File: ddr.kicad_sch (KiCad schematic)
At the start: 79 parts, among them U801 MT41K256M16TW

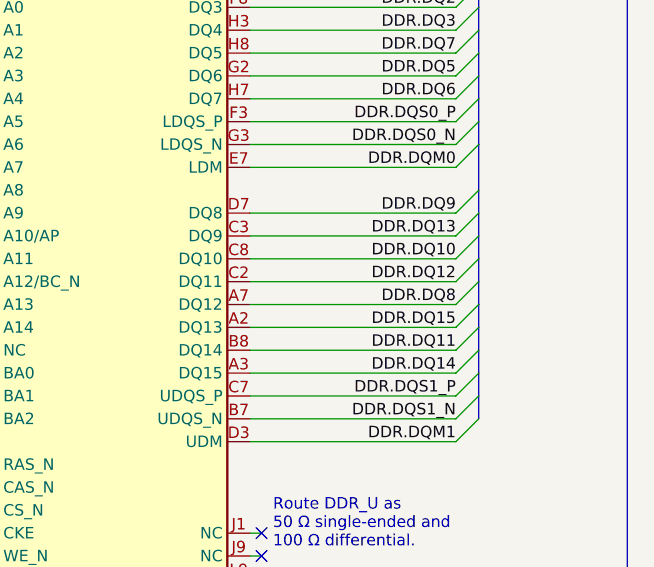
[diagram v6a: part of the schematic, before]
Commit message: Finish cleaner DDR routing
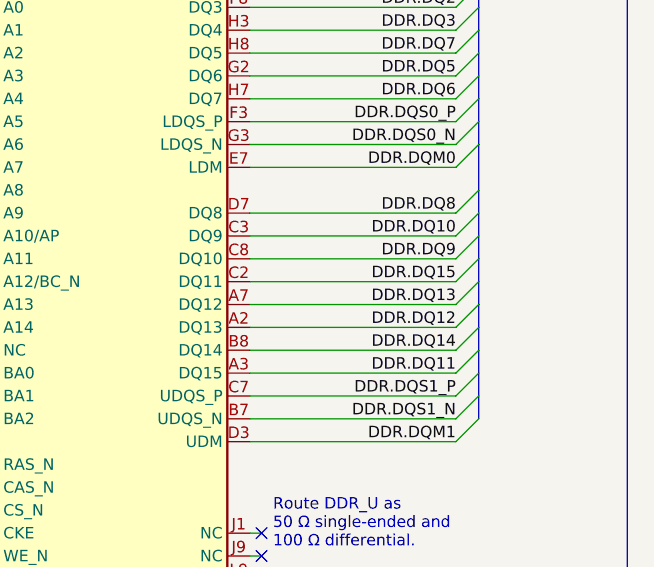
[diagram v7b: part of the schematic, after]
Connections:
- net DDR.DQ10: now also U801.C3 (DQ9); no longer U801.C8 (DQ10)
- net DDR.DQ11: now also U801.A3 (DQ15); no longer U801.B8 (DQ14)
- net DDR.DQ12: now also U801.A2 (DQ13); no longer U801.C2 (DQ11)
- net DDR.DQ13: now also U801.A7 (DQ12); no longer U801.C3 (DQ9)
- net DDR.DQ14: now also U801.B8 (DQ14); no longer U801.A3 (DQ15)
- net DDR.DQ15: now also U801.C2 (DQ11); no longer U801.A2 (DQ13)
- net DDR.DQ8: now also U801.D7 (DQ8); no longer U801.A7 (DQ12)
- net DDR.DQ9: now also U801.C8 (DQ10); no longer U801.D7 (DQ8)
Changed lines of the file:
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@@
 	)
 	(label "DDR.DQ13"
-		(at 387.35 132.08 180)
+		(at 387.35 139.7 180)
 		(effects
 			(font
@@
 	)
 	(label "DDR.DQ12"
-		(at 387.35 137.16 180)
+		(at 387.35 142.24 180)
 		(effects
 			(font
@@
 	)
 	(label "DDR.DQ14"
-		(at 387.35 147.32 180)
+		(at 387.35 144.78 180)
 		(effects
 			(font
@@
 	)
 	(label "DDR.DQ9"
-		(at 387.35 129.54 180)
+		(at 387.35 134.62 180)
 		(effects
 			(font
@@
 	)
 	(label "DDR.DQ11"
-		(at 387.35 144.78 180)
+		(at 387.35 147.32 180)
 		(effects
 			(font
@@
 	)
 	(label "DDR.DQ10"
-		(at 387.35 134.62 180)
+		(at 387.35 132.08 180)
 		(effects
 			(font
@@
 	)
 	(label "DDR.DQ15"
-		(at 387.35 142.24 180)
+		(at 387.35 137.16 180)
 		(effects
 			(font
@@
 	)
 	(label "DDR.DQ8"
-		(at 387.35 139.7 180)
-		(effects
-			(font
+		(at 387.35 129.54 180)
+		(effects
+			(font

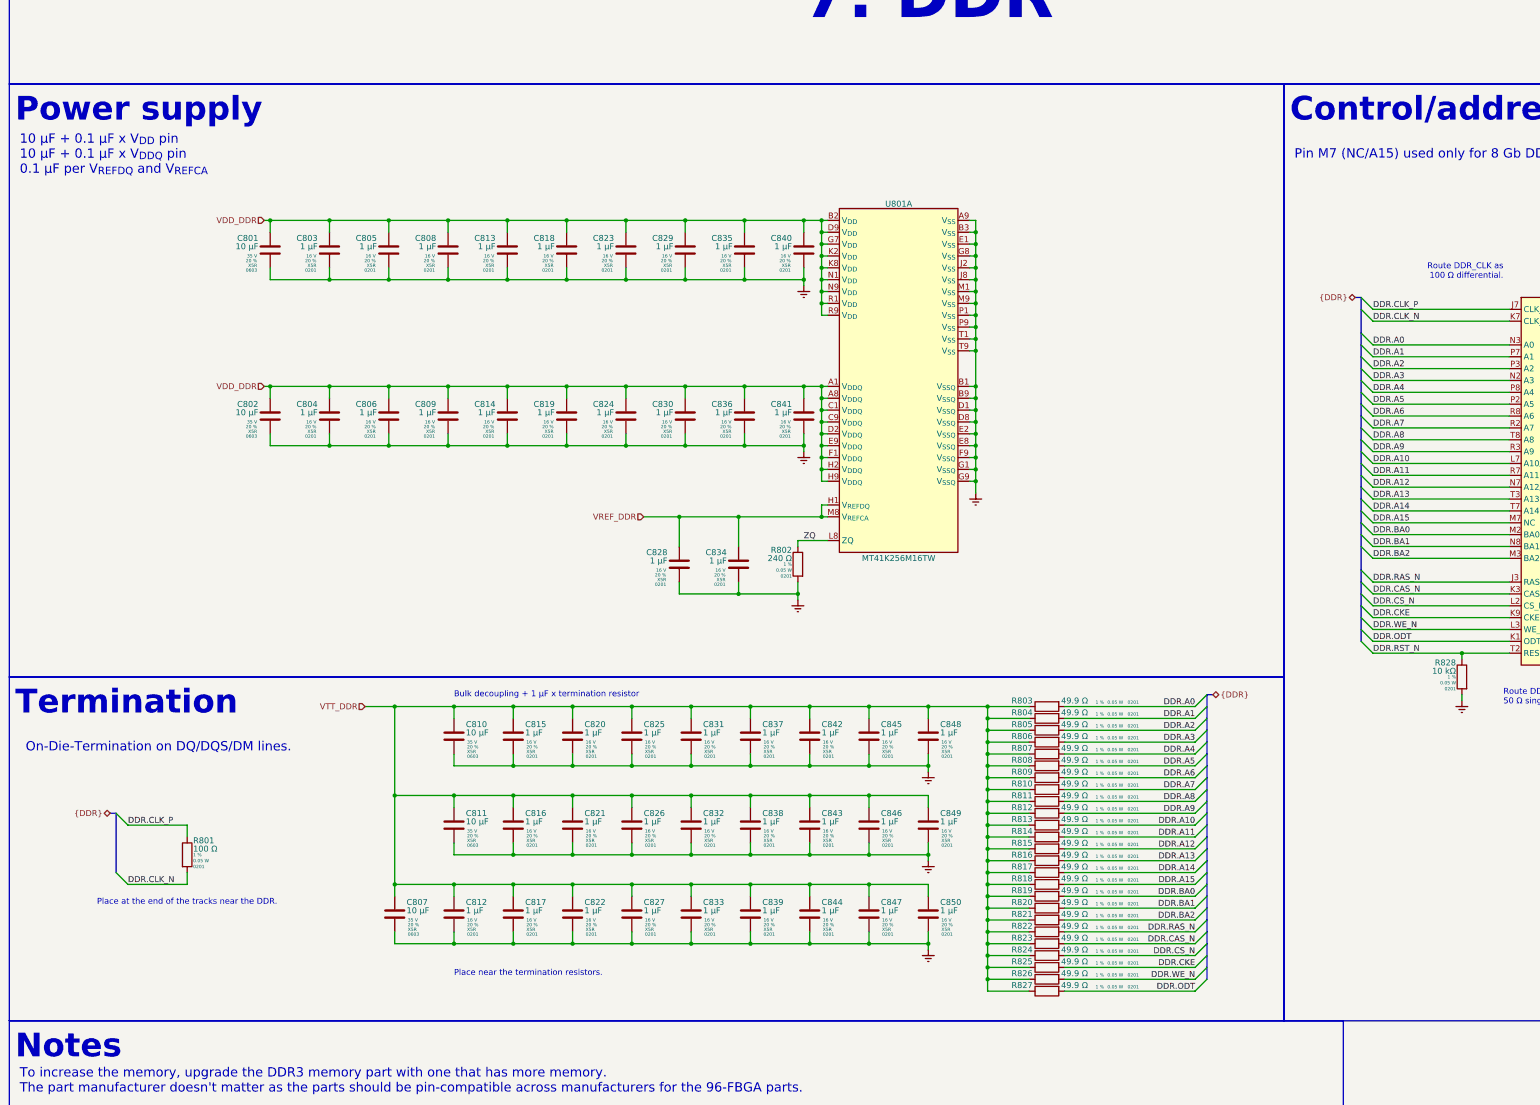
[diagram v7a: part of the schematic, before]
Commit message: Fallback to DDR series termination
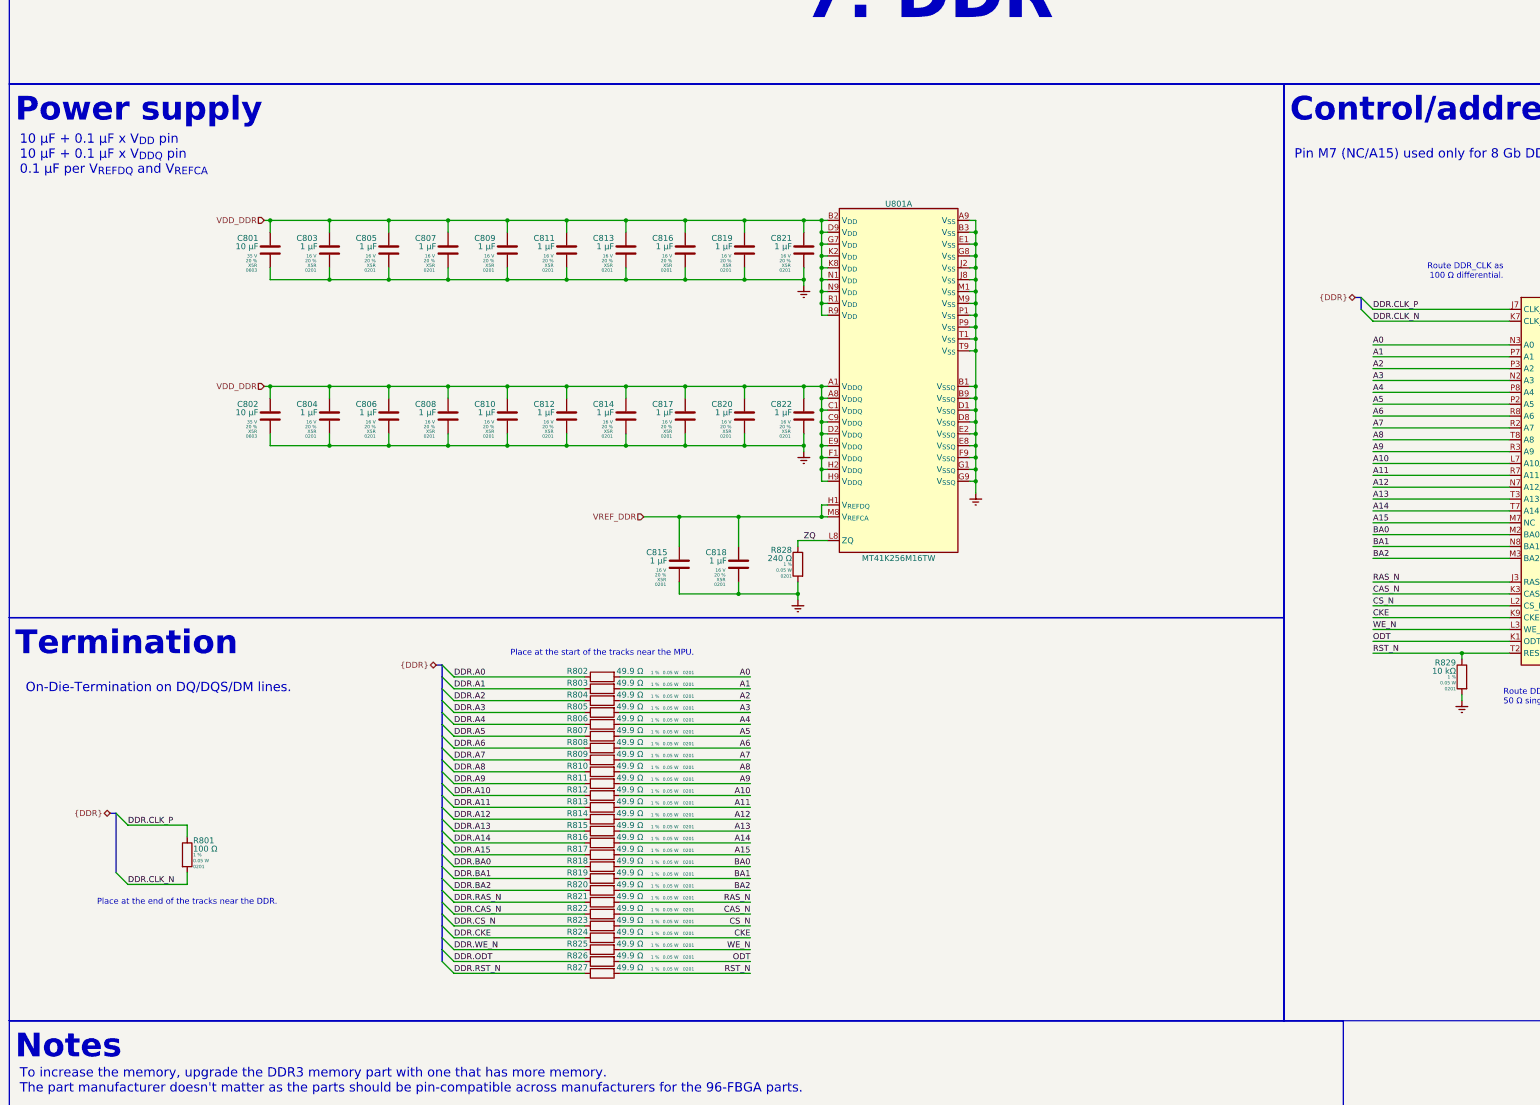
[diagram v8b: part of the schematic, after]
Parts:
- removed C807, C810, C811: 10 µF, Capacitor_SMD:C_0603_1608Metric, symbol Device:C
- removed C812, C815, C816, C817, C820, C821, C822, C825, C826, C827, C831, C832, C833, C837, C838, C839, C842, C843, C844, C845, C846, C847, C848, C849, C850: 1 µF, perfect_footprints:C_0201_0603Metric, symbol Device:C
- added R827: 49.9 Ω, perfect_footprints:R_0201_0603Metric, symbol Device:R
- renumbered C808 to C807, C809 to C808, C813 to C809, C814 to C810, C818 to C811, C819 to C812, C823 to C813, C824 to C814, C828 to C815, C829 to C816, C830 to C817, C834 to C818, C835 to C819, C836 to C820, C840 to C821, C841 to C822, R803 to R802, R804 to R803, R805 to R804, R806 to R805, R807 to R806, R808 to R807, R809 to R808, R810 to R809, R811 to R810, R812 to R811, R813 to R812, R814 to R813, R815 to R814, R816 to R815, R817 to R816, R818 to R817, R819 to R818, R820 to R819, R821 to R820, R822 to R821, R823 to R822, R824 to R823, R825 to R824, R826 to R825, R827 to R826, R802 to R828, R828 to R829
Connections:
- net DDR.A0: now also R802.1; no longer R802.2, U801.N3 (A0)
- net DDR.A1: now also R803.1; no longer R803.2, U801.P7 (A1)
- net DDR.A10: now also R812.1; no longer R812.2, U801.L7 (A10/AP)
- net DDR.A11: now also R813.1; no longer R813.2, U801.R7 (A11)
- net DDR.A12: now also R814.1; no longer R814.2, U801.N7 (A12/BC_N)
- net DDR.A13: now also R815.1; no longer R815.2, U801.T3 (A13)
- net DDR.A14: now also R816.1; no longer R816.2, U801.T7 (A14)
- net DDR.A15: now also R817.1; no longer R817.2, U801.M7 (NC)
- net DDR.A2: now also R804.1; no longer R804.2, U801.P3 (A2)
- net DDR.A3: now also R805.1; no longer R805.2, U801.N2 (A3)
- net DDR.A4: now also R806.1; no longer R806.2, U801.P8 (A4)
- net DDR.A5: now also R807.1; no longer R807.2, U801.P2 (A5)
- net DDR.A6: now also R808.1; no longer R808.2, U801.R8 (A6)
- net DDR.A7: now also R809.1; no longer R809.2, U801.R2 (A7)
- net DDR.A8: now also R810.1; no longer R810.2, U801.T8 (A8)
- net DDR.A9: now also R811.1; no longer R811.2, U801.R3 (A9)
- net DDR.BA0: now also R818.1; no longer R818.2, U801.M2 (BA0)
- net DDR.BA1: now also R819.1; no longer R819.2, U801.N8 (BA1)
- net DDR.BA2: now also R820.1; no longer R820.2, U801.M3 (BA2)
- net DDR.CAS_N: now also R822.1; no longer R822.2, U801.K3 (CAS_N)
- net DDR.CKE: now also R824.1; no longer R824.2, U801.K9 (CKE)
- net DDR.CS_N: now also R823.1; no longer R823.2, U801.L2 (CS_N)
- net DDR.ODT: now also R826.1; no longer R826.2, U801.K1 (ODT)
- net DDR.RAS_N: now also R821.1; no longer R821.2, U801.J3 (RAS_N)
- net DDR.RST_N: now also R827.1; no longer R829.1, U801.T2 (RESET_N)
- net DDR.WE_N: now also R825.1; no longer R825.2, U801.L3 (WE_N)
- removed net VTT_DDR: R802.1, R803.1, R804.1, R805.1, R806.1, R807.1, R808.1, R809.1, R810.1, R811.1, R812.1, R813.1, R814.1, R815.1, R816.1, R817.1, R818.1, R819.1, R820.1, R821.1, R822.1, R823.1, R824.1, R825.1, R826.1
- new net A0: R802.2, U801.N3 (A0)
- new net A1: R803.2, U801.P7 (A1)
- new net A10: R812.2, U801.L7 (A10/AP)
- new net A11: R813.2, U801.R7 (A11)
- new net A12: R814.2, U801.N7 (A12/BC_N)
- new net A13: R815.2, U801.T3 (A13)
- new net A14: R816.2, U801.T7 (A14)
- new net A15: R817.2, U801.M7 (NC)
- new net A2: R804.2, U801.P3 (A2)
- new net A3: R805.2, U801.N2 (A3)
- new net A4: R806.2, U801.P8 (A4)
- new net A5: R807.2, U801.P2 (A5)
- new net A6: R808.2, U801.R8 (A6)
- new net A7: R809.2, U801.R2 (A7)
- new net A8: R810.2, U801.T8 (A8)
- new net A9: R811.2, U801.R3 (A9)
- new net BA0: R818.2, U801.M2 (BA0)
- new net BA1: R819.2, U801.N8 (BA1)
- new net BA2: R820.2, U801.M3 (BA2)
- new net CAS_N: R822.2, U801.K3 (CAS_N)
- new net CKE: R824.2, U801.K9 (CKE)
- new net CS_N: R823.2, U801.L2 (CS_N)
- new net ODT: R826.2, U801.K1 (ODT)
- new net RAS_N: R821.2, U801.J3 (RAS_N)
- new net RST_N: R827.2, R829.1, U801.T2 (RESET_N)
- new net WE_N: R825.2, U801.L3 (WE_N)
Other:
- note added: "Place at the start of the tracks near the MPU."
- note removed: "Bulk decoupling + 1 µF x termination resistor"
- note removed: "Place near the termination resistors."
- moved on the sheet: R802, R803, R804, R805, R806, R807, R808, R809, R810, R811, R812, R813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
